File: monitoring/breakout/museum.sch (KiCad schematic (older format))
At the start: 14 parts, among them CON1 UNREG_VIN, J1 RJ45_TRACER, P1 CONN_13X2, P2 I2C_2, P3 I2C_1, P4 12V_LOAD, P5 5V_LOAD, Q1 IRFZ44N, Q2 IRFZ44N, U1 LM7812CT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

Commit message: Updates board
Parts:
- removed R1: 10K, Resistors_SMD:R_1206_HandSoldering, symbol R
- added R?: 10K, Resistors_SMD:R_1206_HandSoldering, symbol R
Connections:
- net +5V: now also R?.2
- net RASPI_GPIO_24: now also Q1.1 (G), R?.1
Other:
- note added: "0.2"
- note added: "The Mµseum Raspi Control Board"
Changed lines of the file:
@@
 EESchema Schematic File Version 2
-LIBS:museum-rescue
 LIBS:power
 LIBS:device
@@
 Text GLabel 7700 3250 2    60   Output ~ 0
 RASPI_TXD
-Wire Wire Line
-	6900 3250 7700 3250
 Text GLabel 6900 3350 2    60   Input ~ 0
 RASPI_RXD
@@
 Text GLabel 9300 4850 3    60   UnSpc ~ 0
 TRACER_12V
-Wire Wire Line
-	9700 4700 9700 4850
-Wire Wire Line
-	9800 4700 9800 5500
-Wire Wire Line
-	9200 4700 9200 5500
-Wire Wire Line
-	9300 4700 9300 4850
-Wire Wire Line
-	9100 4700 9100 4850
 Text GLabel 9500 4850 3    60   Output ~ 0
 TRACER_TXD
 Text GLabel 9600 5500 3    60   Input ~ 0
 TRACER_RXD
-Wire Wire Line
-	9600 5500 9600 4700
-Wire Wire Line
-	9500 4700 9500 4850
 Text GLabel 6350 4450 0    60   Output ~ 0
 RASPI_TXD
@@
 Text GLabel 6650 4450 2    60   Input ~ 0
 TRACER_RXD
-Wire Wire Line
-	6350 4600 6650 4600
-Wire Wire Line
-	6650 4450 6350 4450
-Wire Wire Line
-	10000 3900 10000 4100
-Wire Wire Line
-	5350 3250 6100 3250
-Wire Wire Line
-	6100 3050 5350 3050
 $Comp
 L LM7812CT U1
@@
 	1    0    0    -1
 $EndComp
-Wire Wire Line
-	2000 4400 2000 4550
-Wire Wire Line
-	2400 4100 2550 4100
 Text GLabel 9100 4850 3    60   UnSpc ~ 0
 TRACER_12V
-Wire Wire Line
-	1500 4100 1600 4100
 Text GLabel 1500 4100 0    60   Input ~ 0
 12V_BATT
@@
 	1    0    0    -1
 $EndComp
-Wire Wire Line
-	1850 1000 1550 1000
-Wire Wire Line
-	1550 1200 1850 1200
 Text GLabel 1500 3700 0    60   Input ~ 0
 12V_BATT
@@
 	1    0    0    -1
 $EndComp
-Wire Wire Line
-	2100 3700 2550 3700
-Wire Wire Line
-	2550 3700 2550 3600
-Wire Wire Line
-	1550 1100 1650 1100
-Wire Wire Line
-	1650 1100 1650 1200
-Connection ~ 1650 1200
-Wire Wire Line
-	1900 3700 1500 3700
-Wire Wire Line
-	9400 4700 9400 5500
 $Comp
 L R-785 U2
@@
 	1    0    0    -1
 $EndComp
-Wire Wire Line
-	9200 3400 9450 3400
-Wire Wire Line
-	9200 3300 9950 3300
-Wire Wire Line
-	9200 3200 9450 3200
-Wire Wire Line
-	9200 3100 9450 3100
 Text GLabel 9450 3400 2    60   UnSpc ~ 0
 +3.3V
@@
 	1    0    0    -1
 $EndComp
-Wire Wire Line
-	9200 2800 9950 2800
-Wire Wire Line
-	9200 2900 9450 2900
-Wire Wire Line
-	9200 2700 9450 2700
-Wire Wire Line
-	9200 2600 9450 2600
 $Comp
 L GND #PWR017
@@
 Text GLabel 1750 2750 0    60   Input ~ 0
 12V_BATT
-Wire Wire Line
-	1750 2750 1900 2750
-Wire Wire Line
-	1900 2750 1900 2650
 $Comp
 L GND #PWR018
@@
 Text GLabel 7100 2950 2    60   Input ~ 0
 RASPI_5V
-Wire Wire Line
-	6900 2950 6900 3050
-Wire Wire Line
-	6900 2950 7100 2950
 Text GLabel 2200 2750 2    60   Input ~ 0
 RASPI_5V
-Wire Wire Line
-	2100 2650 2100 2750
-Wire Wire Line
-	2100 2750 2200 2750
 $Comp
 L IRF540N Q1
@@
 	-1   0    0    1
 $EndComp
-$Comp
-L R R1
-U 1 1 5563E3B0
-P 3300 1950
-F 0 "R1" V 3380 1950 50  0000 C CNN
-F 1 "10K" V 3300 1950 50  0000 C CNN
-F 2 "Resistors_SMD:R_1206_HandSoldering" V 3230 1950 30  0001 C CNN
-F 3 "" H 3300 1950 30  0000 C CNN
-	1    3300 1950
-	-1   0    0    1
-$EndComp
 Text GLabel 6050 3750 0    60   UnSpc ~ 0
 +3.3V
-Wire Wire Line
-	6050 3750 6100 3750
 $Comp
 L R R2
@@
 Text GLabel 5350 3650 0    60   BiDi ~ 0
 RASPI_GPIO_22
-Wire Wire Line
-	5350 3650 6100 3650
-Wire Wire Line
-	5350 3450 6100 3450
 Text GLabel 7700 3650 2    60   BiDi ~ 0
 RASPI_GPIO_23
 Text GLabel 6900 3750 2    60   BiDi ~ 0
 RASPI_GPIO_24
-Wire Wire Line
-	7700 3650 6900 3650
 Text GLabel 7700 3450 2    60   BiDi ~ 0
 RASPI_GPIO_18
-Wire Wire Line
-	7700 3450 6900 3450
 Text GLabel 7700 3950 2    60   BiDi ~ 0
 RASPI_GPIO_25
@@
 Text GLabel 7700 4150 2    60   BiDi ~ 0
 RASPI_GPIO_07
-Wire Wire Line
-	7700 4150 6900 4150
-Wire Wire Line
-	6900 3950 7700 3950
 Text GLabel 5350 3850 0    60   BiDi ~ 0
 RASPI_GPIO_10
@@
 Text GLabel 5350 4050 0    60   BiDi ~ 0
 RASPI_GPIO_08
-Wire Wire Line
-	5350 3850 6100 3850
-Wire Wire Line
-	6100 4050 5350 4050
-Text GLabel 3300 2100 3    60   Input ~ 0
+Text GLabel 3100 1900 3    60   Input ~ 0
 RASPI_GPIO_24
 $Comp
@@
 	0    -1   -1   0
 $EndComp
-Wire Wire Line
-	3600 1150 3600 1550
 $Comp
 L CONN_01X02 P5
@@
 	0    -1   -1   0
 $EndComp
-Wire Wire Line
-	4750 1150 4750 1550
 Text Label 3600 1400 0    60   ~ 0
 12V_GND_SW
 Text Label 4750 1400 0    60   ~ 0
 5V_GND_SW
+$Comp
+L +5V #PWR?
+U 1 1 557A6041
+P 3100 1400
+F 0 "#PWR?" H 3100 1250 50  0001 C CNN
+F 1 "+5V" H 3100 1540 50  0000 C CNN
+F 2 "" H 3100 1400 60  0000 C CNN
+F 3 "" H 3100 1400 60  0000 C CNN
+	1    3100 1400
+	1    0    0    -1
+$EndComp
+$Comp
+L R R?
+U 1 1 557A607D
+P 3100 1550
+F 0 "R?" V 3180 1550 50  0000 C CNN
+F 1 "10K" V 3100 1550 50  0000 C CNN
+F 2 "Resistors_SMD:R_1206_HandSoldering" V 3030 1550 30  0001 C CNN
+F 3 "" H 3100 1550 30  0000 C CNN
+	1    3100 1550
+	-1   0    0    1
+$EndComp
+Wire Wire Line
+	6900 3250 7700 3250
+Wire Wire Line
+	9700 4700 9700 4850
+Wire Wire Line
+	9800 4700 9800 5500
+Wire Wire Line
+	9200 4700 9200 5500
+Wire Wire Line
+	9300 4700 9300 4850
+Wire Wire Line
+	9100 4700 9100 4850
+Wire Wire Line
+	9600 5500 9600 4700
+Wire Wire Line
+	9500 4700 9500 4850
+Wire Wire Line
+	6350 4600 6650 4600
+Wire Wire Line
+	6650 4450 6350 4450
+Wire Wire Line
+	10000 3900 10000 4100
+Wire Wire Line
+	5350 3250 6100 3250
+Wire Wire Line
+	6100 3050 5350 3050
+Wire Wire Line
+	2000 4400 2000 4550
+Wire Wire Line
+	2400 4100 2550 4100
+Wire Wire Line
+	1500 4100 1600 4100
+Wire Wire Line
+	1850 1000 1550 1000
+Wire Wire Line
+	1550 1200 1850 1200
+Wire Wire Line
+	2100 3700 2550 3700
+Wire Wire Line
+	2550 3700 2550 3600
+Wire Wire Line
+	1550 1100 1650 1100
+Wire Wire Line
+	1650 1100 1650 1200
+Connection ~ 1650 1200
+Wire Wire Line
+	1900 3700 1500 3700
+Wire Wire Line
+	9400 4700 9400 5500
+Wire Wire Line
+	9200 3400 9450 3400
+Wire Wire Line
+	9200 3300 9950 3300
+Wire Wire Line
+	9200 3200 9450 3200
+Wire Wire Line
+	9200 3100 9450 3100
+Wire Wire Line
+	9200 2800 9950 2800
+Wire Wire Line
+	9200 2900 9450 2900
+Wire Wire Line
+	9200 2700 9450 2700
+Wire Wire Line
+	9200 2600 9450 2600
+Wire Wire Line
+	1750 2750 1900 2750
+Wire Wire Line
+	1900 2750 1900 2650
+Wire Wire Line
+	6900 2950 6900 3050
+Wire Wire Line
+	6900 2950 7100 2950
+Wire Wire Line
+	2100 2650 2100 2750
+Wire Wire Line
+	2100 2750 2200 2750
+Wire Wire Line
+	6050 3750 6100 3750
+Wire Wire Line
+	5350 3650 6100 3650
+Wire Wire Line
+	5350 3450 6100 3450
+Wire Wire Line
+	7700 3650 6900 3650
+Wire Wire Line
+	7700 3450 6900 3450
+Wire Wire Line
+	7700 4150 6900 4150
+Wire Wire Line
+	6900 3950 7700 3950
+Wire Wire Line
+	5350 3850 6100 3850
+Wire Wire Line
+	6100 4050 5350 4050
+Wire Wire Line
+	3600 1150 3600 1550
+Wire Wire Line
+	4750 1150 4750 1550
+Wire Wire Line
+	3100 1700 3100 1900
+Wire Wire Line
+	3100 1800 3300 1800
+Connection ~ 3100 1800
+Text Notes 8850 7500 2    60   ~ 0
+The Mµseum Raspi Control Board
+Text Notes 10700 7650 2    60   ~ 0
+0.2
 $EndSCHEMATC

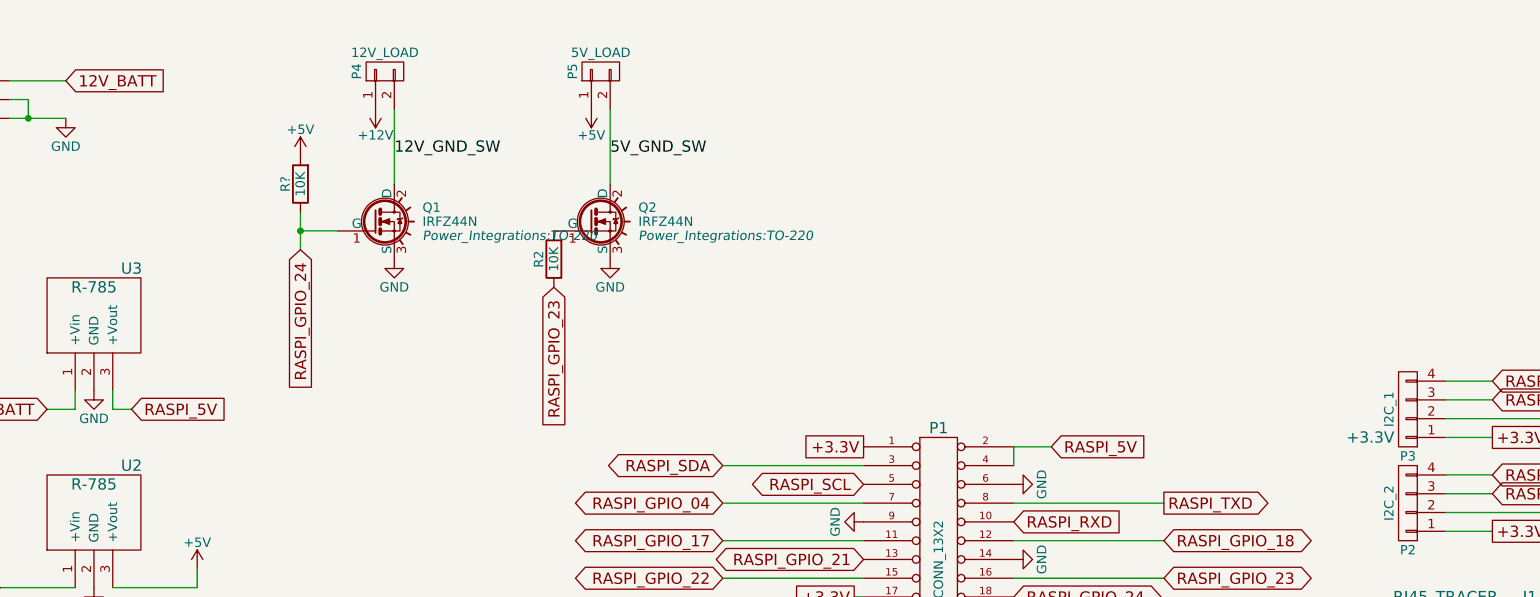
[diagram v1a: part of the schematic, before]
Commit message: Control board revisions (v0.2)
* Fix RECOM footprints
* Replace MOSFETs with ones whose gate threshold will work for the 3.3v
  Raspi GPIOs
* Add second 12v MOSFET-switched channel to the Raspi GPIO with PWM
* Output channels: move from tiny connectors to ones that should be
  better suited for higher-power use (also one that has screw terminals)
* Replace barrel jack pad slots (which OSH Park doesn't support) with
  holes
* Made board bigger and relaid parts to fit new connectors
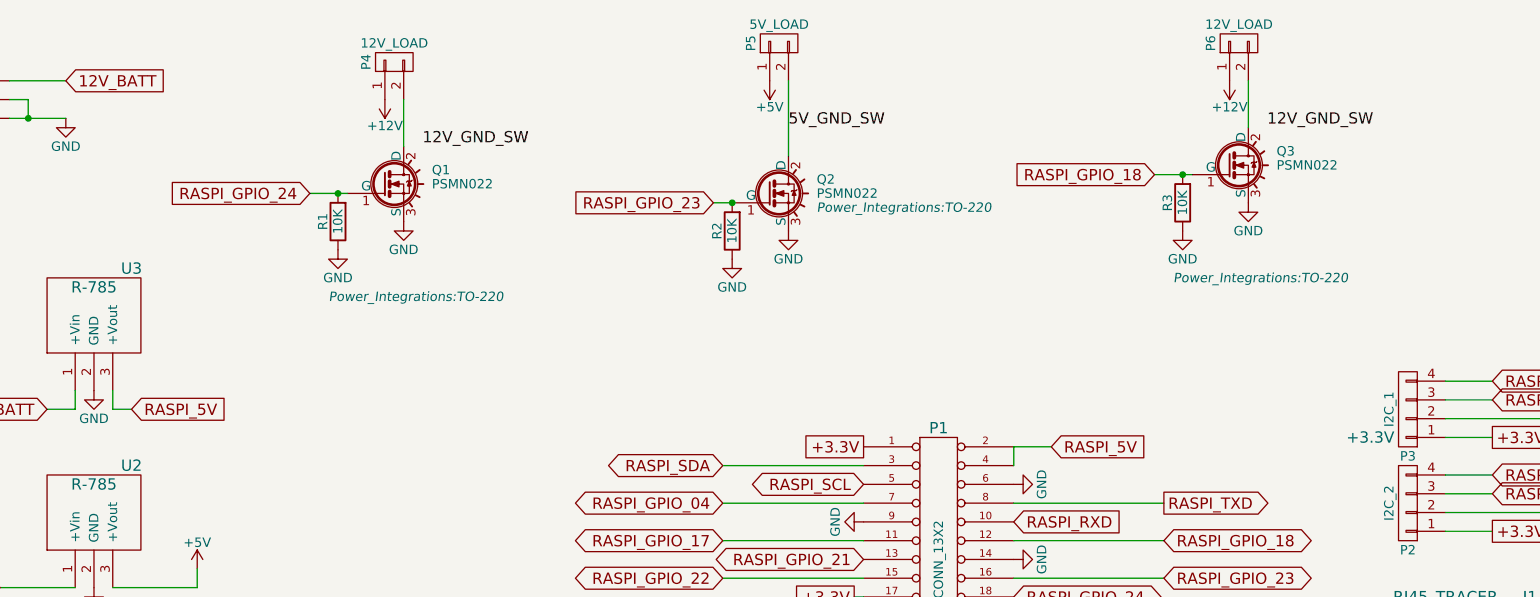
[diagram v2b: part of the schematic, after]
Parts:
- added P6: 12V_LOAD, connector:OSTOQ027151, symbol CONN_01X02
- added Q3: PSMN022, Power_Integrations:TO-220, symbol IRF540N
- added R3: 10K, Resistors_SMD:R_1206_HandSoldering, symbol R
- P4, P5: footprint Connectors_Molex:Connector_Molex_PicoBlade_53048-0210 -> connector:OSTOQ027151
- Q1, Q2: value IRFZ44N -> PSMN022
- U2, U3: footprint Converters_DCDC_ACDC:DCDC-Conv_Recom_R-78HBxx-0.5 -> dc_dc:RECOM_R-78xx
- gave numbers to parts that had none: 1
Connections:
- net +12V: now also P6.1 (P1)
- net +5V: no longer R1.2
- net 12V_GND_SW: no longer P4.2 (P2), Q1.2 (D)
- net GND: now also R1.1, R2.1, Q3.3 (S), R3.1
- net RASPI_GPIO_18: now also Q3.1 (G), R3.2
- net RASPI_GPIO_23: now also Q2.1 (G), R2.2; no longer R2.1
- net RASPI_GPIO_24: now also R1.2; no longer R1.1
- new net: P4.2 (P2), Q1.2 (D)
- new net: P6.2 (P2), Q3.2 (D)
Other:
- moved on the sheet: P5, Q1, Q2, R1, R2

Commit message: Correct text labels
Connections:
- net 12V_SW_01: now reaches P4.2 (P2), Q1.2 (D)
- net 12V_SW_02: now reaches P6.2 (P2), Q3.2 (D)
- net 5V_GND_SW renamed 5V_SW_01
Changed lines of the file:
@@
 	0    -1   -1   0
 $EndComp
-Text Label 3750 1350 0    60   ~ 0
-12V_GND_SW
-Text Label 5700 1250 0    60   ~ 0
-5V_GND_SW
 $Comp
 L R R1
@@
 Text GLabel 7650 1500 0    60   Input ~ 0
 RASPI_GPIO_18
-Text Label 8250 1250 0    60   ~ 0
-12V_GND_SW
 $Comp
 L R R3
@@
 $EndComp
 Connection ~ 7800 1500
+Text Label 3650 1200 0    60   ~ 0
+12V_SW_01
+Text Label 5700 1100 0    60   ~ 0
+5V_SW_01
+Text Label 8150 1100 0    60   ~ 0
+12V_SW_02
 $EndSCHEMATC
